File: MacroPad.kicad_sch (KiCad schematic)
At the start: 29 parts, among them SW1 RotaryEncoder_Switch, SW12 RotaryEncoder_Switch, SW2 RotaryEncoder_Switch, U1 Pico

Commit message: Redid the schematic should be finished
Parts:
- removed D1, D2, D3, D4, D5, D6, D7, D8, D9: Diode, s_components:Diode_DO-35, symbol Scotto keedbs:Placeholder_Diode
- removed R5, R6: R, Resistor_THT:R_Axial_DIN0204_L3.6mm_D1.6mm_P7.62mm_Horizontal, symbol Device:R
- removed SW12: RotaryEncoder_Switch, Rotary_Encoder:RotaryEncoder_Alps_EC11E-Switch_Vertical_H20mm, symbol Device:RotaryEncoder_Switch
- added Brd1: SSD1306, dsada:128x64OLED, symbol dis:SSD1306
- added R7, R8: 10kohm, Resistor_THT:R_Axial_DIN0204_L3.6mm_D1.6mm_P7.62mm_Horizontal, symbol Device:R
- added SW3: RotaryEncoder_Switch, Rotary_Encoder:RotaryEncoder_Alps_EC11E-Switch_Vertical_H20mm, symbol Device:RotaryEncoder_Switch
- R1, R2, R3, R4: value R -> 10kohm
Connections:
- net 3.3V is gone; now on net Toggle2: toggle1.
- net +3.3V: now also R1.1, R2.1, R3.1, R4.1, S1.2, S2.2, S3.2, S4.2, S5.2, S6.2, S7.2, S8.2, S9.2, toggle1., Brd1.2 (VCC), R7.1, R8.1
- net A1: now also SW1.A, U1.15 (GPIO11), R8.2; no longer R2.1, U1.17 (GPIO13)
- net A2: now also R1.2, SW2.A, U1.19 (GPIO14); no longer R4.1, SW1.A, U1.21 (GPIO16)
- net A3: now also R3.2, U1.32 (GPIO27_ADC1), SW3.A; no longer SW2.A, U1.14 (GPIO10)
- net B1: now also SW1.B, R7.2; no longer R1.1
- net B2: now also R2.2, SW2.B; no longer R3.1, SW1.B
- net B3: now also R4.2, U1.31 (GPIO26_ADC0), SW3.B; no longer SW2.B, U1.12 (GPIO9)
- net GND: now also U1.13 (GND), U1.18 (GND), U1.23 (GND), U1.28 (GND), U1.3 (GND), U1.38 (GND), U1.42 (GND), U1.8 (GND), Brd1.1 (GND), SW3.C, SW3.S2
- net SW1: now also SW1.S1, U1.17 (GPIO13); no longer U1.15 (GPIO11)
- net SW2: now also SW2.S1, U1.34 (GPIO28_ADC2); no longer SW1.S1, U1.19 (GPIO14)
- net SW3: now also U1.29 (GPIO22), SW3.S1; no longer SW2.S1, U1.11 (GPIO8)
- net Toggle1: now also U1.12 (GPIO9); no longer U1.10 (GPIO7)
- net Toggle2: now also U1.14 (GPIO10); no longer U1.9 (GPIO6)
- net SCL: now reaches U1.22 (GPIO17)
- net SCL: now also Brd1.3 (SCL)
- removed net +5V: R1.2, R2.2, R3.2, R4.2
- net Col 0 renamed S4
- net S4: no longer S1.1, S7.1
- net Col 1 renamed S5
- net S5: no longer S2.1, S8.1
- net Col 2 renamed S6
- net S6: no longer S3.1, S9.1
- net Row 0 renamed S1
- net S1: now also S1.1
- net Row 1 renamed S2
- net S2: now also S2.1
- net Row 2 renamed S3
- net S3: now also S3.1
- new net S7: S7.1, U1.9 (GPIO6)
- new net S8: S8.1, U1.10 (GPIO7)
- new net S9: S9.1, U1.11 (GPIO8)
- new net SDA: Brd1.4 (SDA), U1.21 (GPIO16)
- no-connect marks 0 -> 12
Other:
- note added: "For ERC purpose only. GND&3V3 supplied by Pi"
- moved on the sheet: U1, toggle1

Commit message: Electric test work
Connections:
- net GND: no longer U1.38 (GND)
- no-connect marks 12 -> 13
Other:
- moved on the sheet: R1, R2, R7, R8, S1, S2, S3, S4, S5, S6, S7, S8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

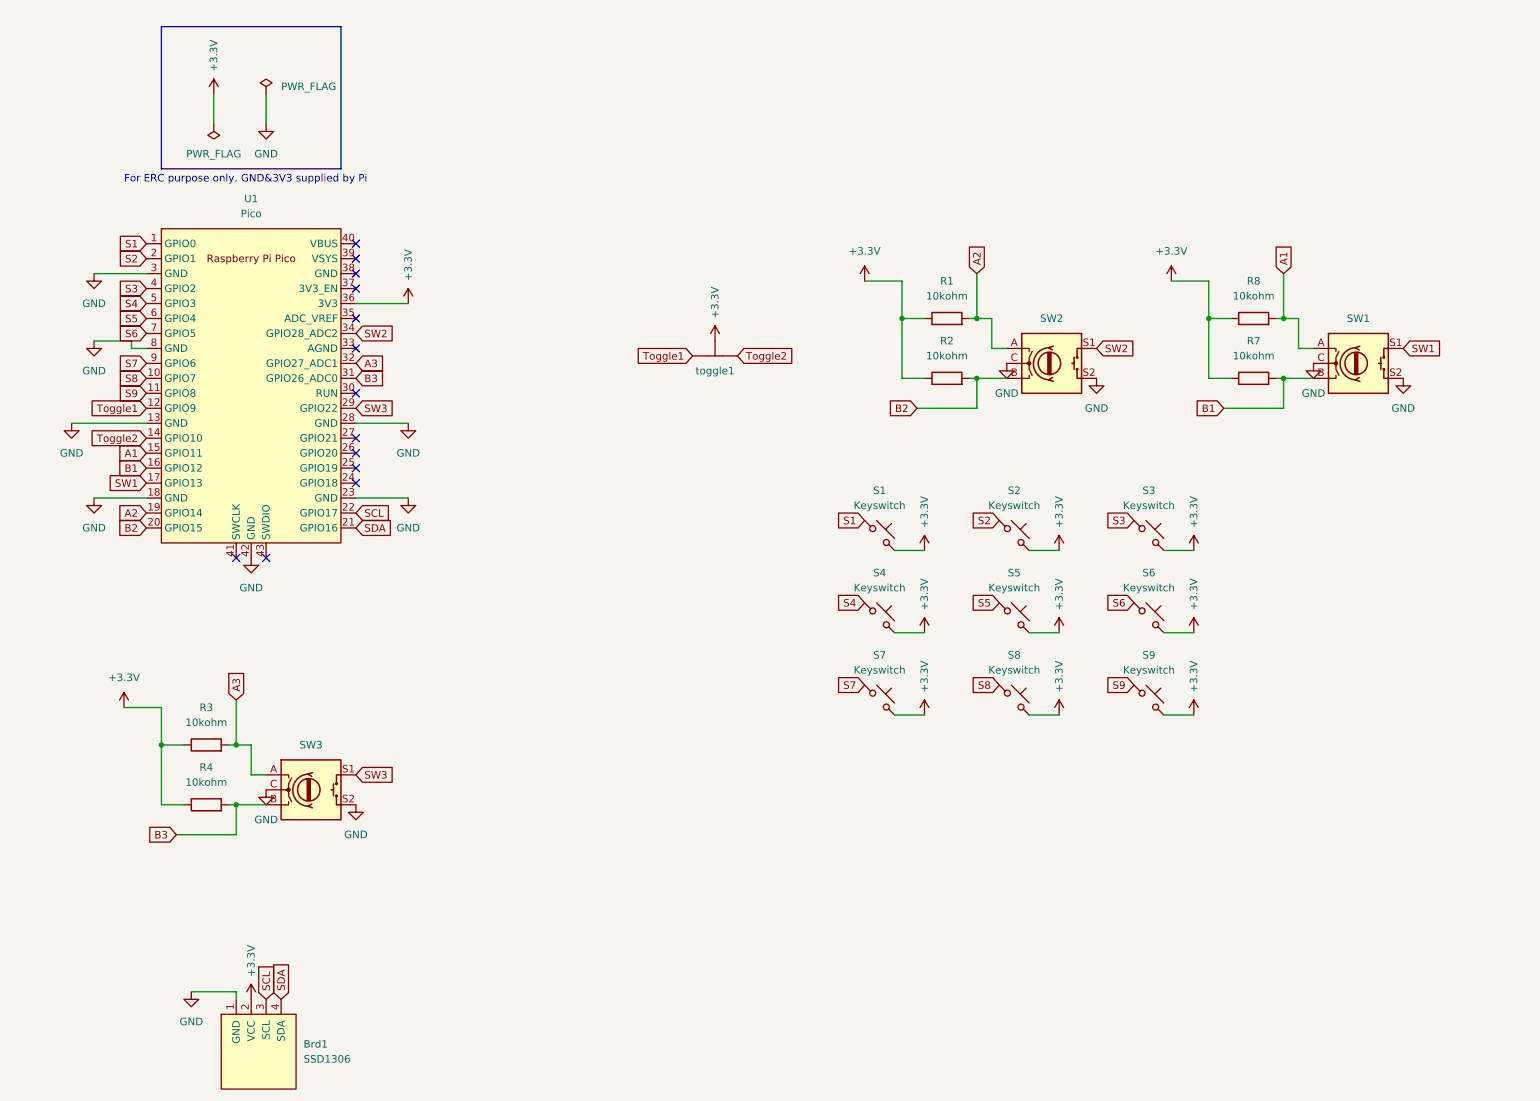
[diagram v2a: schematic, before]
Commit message: Turns out I didn't pull up resistors for the rotary encoder
The pi pico has a PULL_UP for this lol
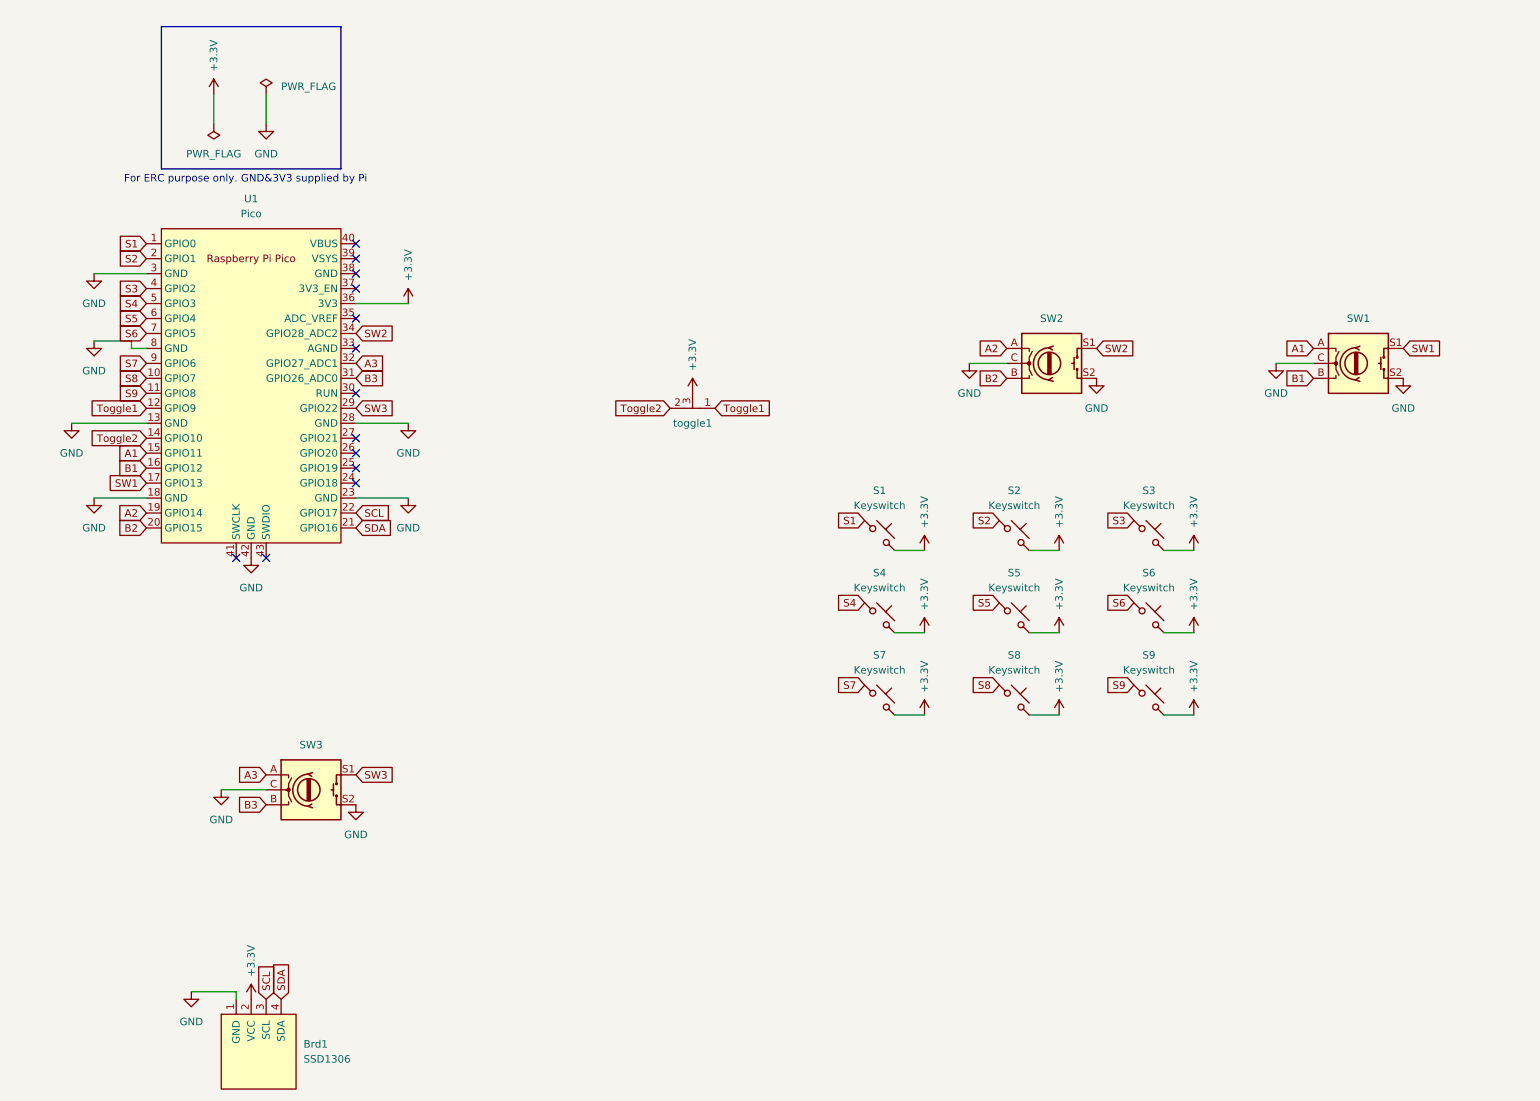
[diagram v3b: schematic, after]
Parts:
- removed R1, R2, R3, R4, R7, R8: 10kohm, Resistor_THT:R_Axial_DIN0204_L3.6mm_D1.6mm_P7.62mm_Horizontal, symbol Device:R
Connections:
- net +3.3V: now also toggle1.3; no longer toggle1.
- net Toggle1: now also toggle1.1; no longer toggle1.
- net Toggle2: now also toggle1.2; no longer toggle1.

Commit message: last schematic update????
Oled screen now hooked up on 5V
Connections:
- net +3.3V: no longer Brd1.2 (VCC)
- net +5V: now reaches U1.39 (VSYS)
- net +5V: now also Brd1.2 (VCC)
- no-connect marks 13 -> 12
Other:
- moved on the sheet: Brd1, SW3
